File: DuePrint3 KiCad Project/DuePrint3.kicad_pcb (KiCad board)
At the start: 2 copper layers, 208.9 x 75.2 mm, 50 parts, among them J1 MF3.0-2x12-430452412, J10 MF3.0-1x2-436500215, J11 2.54Header-1x2-M, J12 2.54Header-1x2-M, J13 EHT-125-01-S-D, J14 EHT-110-01-S-D, J15 EHT-125-01-S-D, J2 2.54Header-1x16-F, J3 2.54Header-1x16-F, J4 6P2C, J5 6P2C, J6 2.54Header-1x3-M, J7 MF3.0-1x2-436500215, J8 MF3.0-1x8-436500815, J9 MF3.0-2x9-430451812, U1 SN74AHCT125DR

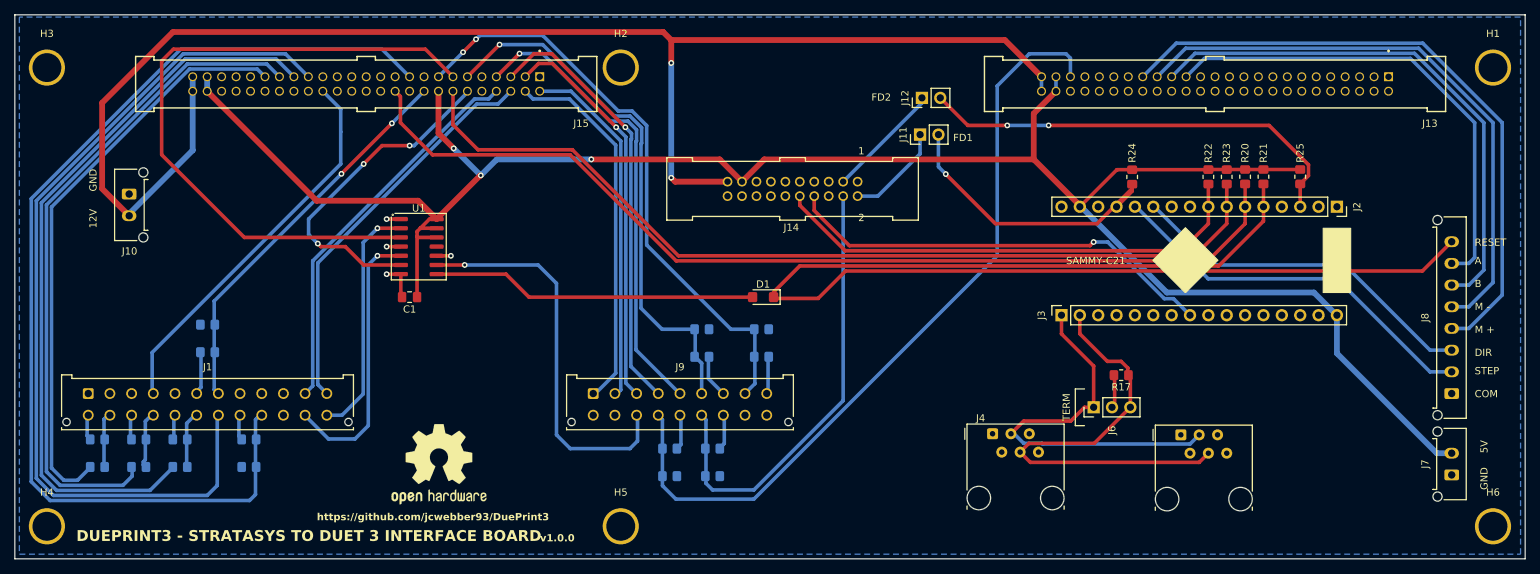
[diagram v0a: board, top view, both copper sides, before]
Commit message: v2.2.0 initial release
Primarily focused on KiCad files, configuration files, build instructions.
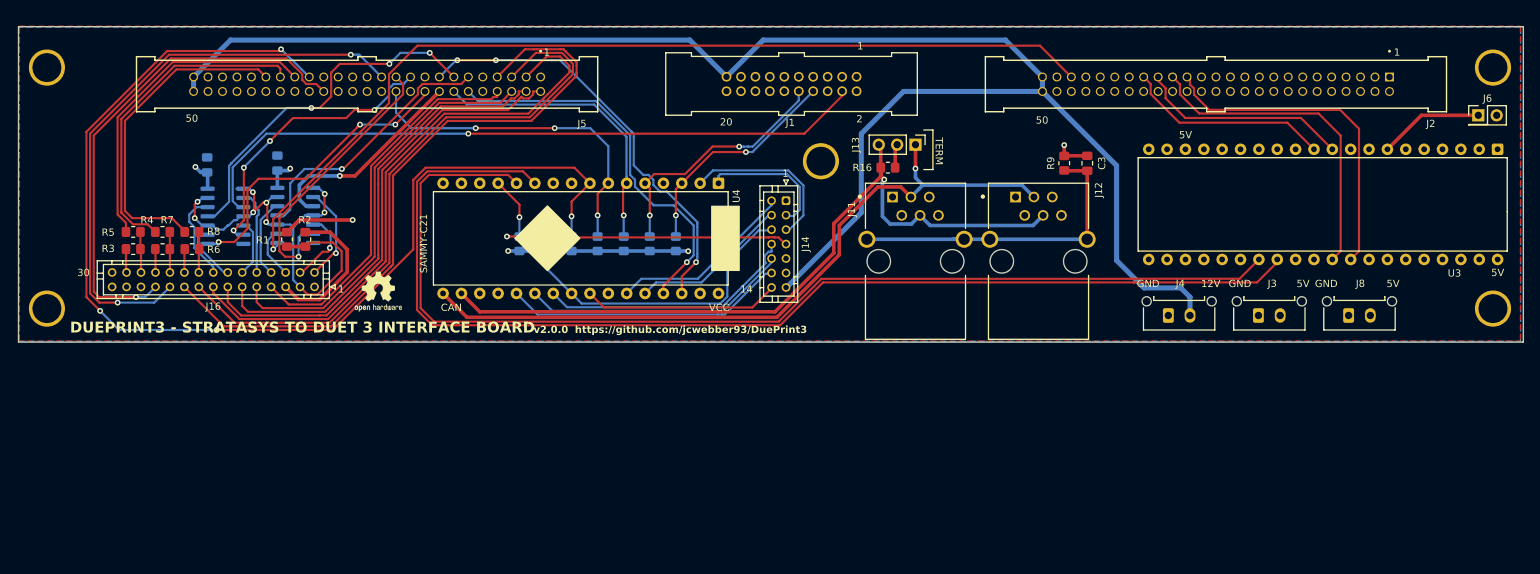
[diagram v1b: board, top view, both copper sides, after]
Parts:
- removed D1: 100v 1A, Diode_SMD:D_SMF
- removed H6: MountingHole_Pad, Stratasys Adapter:MountingHole_4.00mm_Pad
- removed J10, J7: MF3.0-1x2-436500215, Connector_Molex:Molex_Micro-Fit_3.0_43650-0215_1x02_P3.00mm_Vertical
- removed J15: EHT-125-01-S-D, DuePrint3-Lib:SAMTEC_EHT-125-01-S-D
- removed J9: MF3.0-2x9-430451812, Connector_Molex:Molex_Micro-Fit_3.0_43045-1812_2x09_P3.00mm_Vertical
- removed R18: 31.6K, Resistor_SMD:R_0805_2012Metric_Pad1.20x1.40mm_HandSolder
- removed R19: 3740, Resistor_SMD:R_0805_2012Metric_Pad1.20x1.40mm_HandSolder
- removed R20, R21, R22, R23, R24, R25: 10k, Resistor_SMD:R_0805_2012Metric_Pad1.20x1.40mm_HandSolder
- removed the REF** at (114.6, 86.6)
- added C2: 0.1 µF, Capacitor_SMD:C_0805_2012Metric_Pad1.18x1.45mm_HandSolder, B.Cu at (82.5, 45.2)
- added C3: 10n 25V, Capacitor_SMD:C_0805_2012Metric_Pad1.18x1.45mm_HandSolder, F.Cu at (204.2, 45.0)
- added J16: Conn_02x15_Odd_Even, Connector_JST:JST_PHD_B30B-PHDSS_2x15_P2.00mm_Vertical, F.Cu at (97.3, 62.1)
- added REF**: OSHW-Logo2_7.3x6mm_SilkScreen, Symbol:OSHW-Logo2_7.3x6mm_SilkScreen, F.Cu at (106.2, 62.7)
- added U2: SN74AHCT125DR, Package_SO:SOIC-14_3.9x8.7mm_P1.27mm, B.Cu at (85.0, 52.3)
- added U3: BLACKPILL, DuePrint3-Lib:STM32 BLACKPILL, F.Cu at (240.2, 50.5)
- added U4: SAMMY-C21, DuePrint3-Lib:SAMMY-C21, F.Cu at (153.2, 47.8)
- C1: moved to B.Cu
- J1: value MF3.0-2x12-430452412 -> EHT-110-01-S-D; footprint Connector_Molex:Molex_Micro-Fit_3.0_43045-2412_2x12_P3.00mm_Vertical -> DuePrint3-Lib:EHT-110-01-XX-D
- J11, J12: value 2.54Header-1x2-M -> 6P2C; footprint Connector_PinHeader_2.54mm:PinHeader_1x02_P2.54mm_Vertical -> DuePrint3-Lib:BEL_SS-6466S-A-PG1
- J13: value EHT-125-01-S-D -> 2.54Header-1x3-M; footprint DuePrint3-Lib:SAMTEC_EHT-125-01-S-D -> Connector_PinHeader_2.54mm:PinHeader_1x03_P2.54mm_Vertical
- J14: value EHT-110-01-S-D -> Conn_02x07_Top_Bottom; footprint DuePrint3-Lib:EHT-110-01-XX-D -> Connector_JST:JST_PHD_B14B-PHDSS_2x07_P2.00mm_Vertical
- J2: value 2.54Header-1x16-F -> EHT-125-01-S-D; footprint Connector_PinSocket_2.54mm:PinSocket_1x16_P2.54mm_Vertical -> DuePrint3-Lib:SAMTEC_EHT-125-01-S-D
- J3: value 2.54Header-1x16-F -> MF3.0-1x2-436500215; footprint Connector_PinSocket_2.54mm:PinSocket_1x16_P2.54mm_Vertical -> Connector_Molex:Molex_Micro-Fit_3.0_43650-0215_1x02_P3.00mm_Vertical
- J4: value 6P2C -> MF3.0-1x2-436500215; footprint Connector_RJ:RJ12_Amphenol_54601-x06_Horizontal -> Connector_Molex:Molex_Micro-Fit_3.0_43650-0215_1x02_P3.00mm_Vertical
- J5: value 6P2C -> EHT-125-01-S-D; footprint Connector_RJ:RJ12_Amphenol_54601-x06_Horizontal -> DuePrint3-Lib:SAMTEC_EHT-125-01-S-D
- J6: value 2.54Header-1x3-M -> Conn_01x02; footprint Connector_PinHeader_2.54mm:PinHeader_1x03_P2.54mm_Vertical -> Connector_PinHeader_2.54mm:PinHeader_2x01_P2.54mm_Vertical
- J8: value MF3.0-1x8-436500815 -> MF3.0-1x2-436500215; footprint Connector_Molex:Molex_Micro-Fit_3.0_43650-0815_1x08_P3.00mm_Vertical -> Connector_Molex:Molex_Micro-Fit_3.0_43650-0215_1x02_P3.00mm_Vertical
- R1: value 2K -> 3740; moved to F.Cu
- R10, R12, R14: value 3740 -> 10k
- R11, R13, R15: value 31.6K -> 10k
- R16: value 3740 -> 120; moved to F.Cu
- R17: value 120 -> 10k; moved to B.Cu
- R2: value 1K -> 31.6K; moved to F.Cu
- R3, R4, R5: moved to F.Cu
- R6: value 1K -> 2K; moved to F.Cu
- R7: value 31.6K -> 1K; moved to F.Cu
- R8: value 3740 -> 1K; moved to F.Cu
- R9: value 31.6K -> 100K; moved to F.Cu
- U1: footprint PCM_Package_SO_AKL:SOIC-14_3.9x8.7mm_P1.27mm -> Package_SO:SOIC-14_3.9x8.7mm_P1.27mm; moved to B.Cu
- moved H5 124.4 mm to (260.4, 65.1)
- moved J5 122.6 mm to (104.6, 34.1), turned to 180 degrees
- moved R9 121.3 mm to (201.0, 45.0), turned to 90 degrees
- moved J1 106.3 mm to (163.3, 34.0), turned to 180 degrees
- moved R17 81.7 mm to (129.3, 56.1), turned to -90 degrees
- moved R7 76.6 mm to (76.3, 54.5)
- moved R8 71.8 mm to (80.4, 54.5), turned to 180 degrees
- moved J6 66.8 mm to (258.3, 38.4), turned to 0 degrees
- moved R12 60.3 mm to (140.1, 56.1), turned to -90 degrees
- moved R11 55.3 mm to (136.5, 56.1), turned to 90 degrees
- moved R16 52.3 mm to (176.7, 45.6)
- moved R10 51.6 mm to (132.9, 56.1), turned to 90 degrees
- moved J13 42.3 mm to (180.5, 42.4), turned to -90 degrees
- moved R2 39.0 mm to (96.1, 55.5), turned to -90 degrees
- moved R14 35.5 mm to (125.7, 56.1), turned to 90 degrees
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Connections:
- J1 pad 10: unconnected-(J1-Pin_10-Pad10) -> Print Head Support Toggle SW
- J1 pad 11: PRINT BED TOUCH PR LIM SW -> unconnected-(J1-Pin_11-Pad11)
- J1 pad 12: Z-Axis End of Travel Lim SW -> unconnected-(J1-Pin_12-Pad12)
- J1 pad 13: /T0 -> GND
- J1 pad 14: /T0 -> unconnected-(J1-Pin_14-Pad14)
- J1 pad 15: /T2 VSSA -> GND
- J1 pad 16: /T2 -> GND
- J1 pad 17: /T1 VSSA -> +5V
- J1 pad 18: /T1 -> GND
- J1 pad 19: CHAMBER TEMP ALARM -> +12V
- J1 pad 20: VD EXTRUDER SUPPORT HEATER ENABLE -> GND
- J1 pad 4: PRINT HEAD TEMP ALARM -> PRINT HEAD BLOWER ENABLE
- J1 pad 5: unconnected-(J1-Pin_5-Pad5) -> GND
- J1 pad 6: VD EXTRUDER MODEL HEATER ENABLE -> unconnected-(J1-Pin_6-Pad6)
- J1 pad 7: EMHE PWM -> unconnected-(J1-Pin_7-Pad7)
- J1 pad 8: unconnected-(J1-Pin_8-Pad8) -> Print Head Model Toggle SW
- J1 pad 9: unconnected-(J1-Pin_9-Pad9) -> GND
- J11 pad 1: FD1 -> unconnected-(J11-Pad1)
- J11 pad 2: Net-(J11-Pin_2) -> unconnected-(J11-Pad2)
- J12 pad 1: FD2 -> unconnected-(J12-Pad1)
- J12 pad 2: Net-(J12-Pin_2) -> unconnected-(J12-Pad2)
- J13 pad 1: unconnected-(J13-Pin_1-Pad1) -> CAN0H
- J13 pad 2: GND -> Net-(J13-Pin_2)
- J13 pad 3: unconnected-(J13-Pin_3-Pad3) -> CAN0L
- J14 pad 10: Print Head Support Toggle SW -> SPR6
- J14 pad 11: unconnected-(J14-Pin_11-Pad11) -> GND
- J14 pad 12: unconnected-(J14-Pin_12-Pad12) -> SPR7
- J14 pad 13: GND -> +12V
- J14 pad 14: unconnected-(J14-Pin_14-Pad14) -> SPR8
- J14 pad 2: FD1 -> SPR4
- J14 pad 3: FD2 -> SPR1
- J14 pad 4: PHBE PWM -> SPR3
- J14 pad 5: GND -> SPR2
- J14 pad 6: unconnected-(J14-Pin_6-Pad6) -> I_SPR2
- J14 pad 7: unconnected-(J14-Pin_7-Pad7) -> I_SPR1
- J14 pad 8: Print Head Model Toggle SW -> SPR5
- J14 pad 9: GND -> +5V
- J2 pad 10: unconnected-(J2-Pin_10-Pad10) -> GND
- J2 pad 11: DIR -> unconnected-(J2-Pin_11-Pad11)
- J2 pad 12: STEP -> GND
- J2 pad 13: Net-(J11-Pin_2) -> GND
- J2 pad 14: unconnected-(J2-Pin_14-Pad14) -> GND
- J2 pad 15: +5V -> unconnected-(J2-Pin_15-Pad15)
- J2 pad 2: unconnected-(J2-Pin_2-Pad2) -> GND
- J2 pad 3: Net-(J12-Pin_2) -> unconnected-(J2-Pin_3-Pad3)
- J2 pad 4: unconnected-(J2-Pin_4-Pad4) -> GND
- J2 pad 5: GECKO ERROR -> unconnected-(J2-Pin_5-Pad5)
- J2 pad 6: HEAD THERMOSTAT STATUS -> GND
- J2 pad 7: DOOR SWITCH -> unconnected-(J2-Pin_7-Pad7)
- J2 pad 8: Print Head Support Toggle SW -> GND
- J3 pad 1: CAN0H -> GND
- J3 pad 2: CAN0L -> +5V
- J4 pad 1: unconnected-(J4-Pad1) -> GND
- J4 pad 2: unconnected-(J4-Pad2) -> +12V
- J5 pad 1: unconnected-(J5-Pad1) -> GND
- J5 pad 2: unconnected-(J5-Pad2) -> X-Axis End of Travel Lim SW
- J5 pad 3: CAN0H -> X-AXIS HOME LIM SW
- J5 pad 4: CAN0L -> Y-Axis End of Travel Lim SW
- J5 pad 5: unconnected-(J5-Pad5) -> Y-AXIS HOME LIM SW
- J5 pad 6: unconnected-(J5-Pad6) -> Z-Axis End of Travel Lim SW
- J6 pad 1: CAN0H -> Net-(J6-Pin_1)
- J6 pad 2: Net-(J6-Pin_2) -> GND
- J8 pad 2: STEP -> +5V
- R1 pad 1: /T2 VSSA -> 48v RTN PWM
- R1 pad 2: /T2 -> GND
- R10 pad 1: EMHE PWM -> +5V
- R10 pad 2: GND -> CHAMBER TEMP ALARM
- R11 pad 1: VD EXTRUDER SUPPORT HEATER ENABLE -> +5V
- R11 pad 2: ESHE PWM -> HEAD THERMOSTAT STATUS
- R12 pad 1: ESHE PWM -> DOOR SWITCH
- R12 pad 2: GND -> +5V
- R13 pad 1: VD PRINT BED TOUCH PR PWR EN -> Print Head Support Toggle SW
- R13 pad 2: PBTPE PWM -> +5V
- R14 pad 1: PBTPE PWM -> +5V
- R14 pad 2: GND -> I_SPR1
- R15 pad 1: VD MOTOR ENABLE -> +5V
- R15 pad 2: MOTOR ENABLE -> Print Head Model Toggle SW
- R16 pad 1: MOTOR ENABLE -> CAN0L
- R16 pad 2: GND -> Net-(J13-Pin_2)
- R17 pad 1: CAN0L -> +5V
- R17 pad 2: Net-(J6-Pin_2) -> I_SPR2
- R2 pad 1: /T2 -> 48v
- R2 pad 2: PRINT HEAD SUPP THEM -> 48v RTN PWM
- R3 pad 1: /T0 -> /VSSA1
- R3 pad 2: /T0 -> /T1
- R4 pad 1: /T1 VSSA -> /VSSA2
- R4 pad 2: /T1 -> /T2
- R5 pad 2: PRINT HEAD MODEL THEM -> PRINT HEAD MODEL THERM
- R6 pad 1: /T0 -> /VSSA0
- R6 pad 2: CHAMBER TEMP THERM -> /T0
- R7 pad 1: VD CHAMBER HEATER ENABLE -> /T2
- R7 pad 2: CHAMBER HEATER ENABLE -> PRINT HEAD SUPP THERM
- R8 pad 1: CHAMBER HEATER ENABLE -> /T0
- R8 pad 2: GND -> CHAMBER TEMP THERM
- R9 pad 1: VD EXTRUDER MODEL HEATER ENABLE -> Net-(C3-Pad1)
- R9 pad 2: EMHE PWM -> GND
- U1 pad 1: GND -> 48v RTN PWM
- U1 pad 10: GND -> 48v RTN PWM
- U1 pad 11: unconnected-(U1-4Y-Pad11) -> CHAMBER HEATER ENABLE
- U1 pad 12: +5V -> LS CHAMBER HEATER ENABLE
- U1 pad 13: +5V -> 48v RTN PWM
- U1 pad 2: LS DOOR SOLENOID ENABLE -> LS 120V ON
- U1 pad 3: DOOR SOLENOID ENABLE -> 120V ON
- U1 pad 4: GND -> 48v RTN PWM
- U1 pad 5: LS LED Lights Enable -> LS POWER ON
- U1 pad 6: LED Lights Enable -> POWER ON
- U1 pad 8: Net-(D1-A) -> MOTOR ENABLE
- U1 pad 9: LS GECKO RESET -> LS MOTOR ENABLE
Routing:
- net +5V: track 284.3 -> 35.2 mm, vias 3 -> 4
- net GECKO ERROR: track 174.8 -> 0.00 mm
- net ESHE PWM: track 145.5 -> 0.00 mm
- net DIR: track 49.5 -> 159.2 mm
- net PRINT HEAD MODEL THEM: track 102.4 -> 0.00 mm
- net STEP: track 53.3 -> 151.8 mm
- net PRINT HEAD BLOWER ENABLE: track 0.00 -> 95.5 mm, vias 0 -> 1
- net PRINT HEAD SUPP THEM: track 92.4 -> 0.00 mm
- net HEAD THERMOSTAT STATUS: track 137.0 -> 47.3 mm, vias 0 -> 3
- net DOOR SWITCH: track 126.5 -> 40.5 mm, vias 0 -> 1
- net PBTPE PWM: track 82.1 -> 0.00 mm, vias 2 -> 0
- net POWER I/O: track 0.00 -> 80.7 mm, vias 0 -> 2
- net 48v RTN PWM: track 0.00 -> 68.2 mm, vias 0 -> 8
- net PHBE PWM: track 62.2 -> 0.00 mm
- net Net-(J12-Pin_2): track 61.0 -> 0.00 mm, vias 2 -> 0
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- added copper zone on F.Cu, net +5V
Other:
- board size 208.9 x 75.2 mm -> 208.2 x 43.6 mm
- board text added: "1"
- board text added: "14"
- board text added: "20"
- board text added: "30"
- board text added: "50"
- board text added: "CAN"
- board text added: "VCC"
- board text added: "v2.0.0"
- board text removed: "A"
- board text removed: "B"
- board text removed: "COM"
- board text removed: "DIR"
- board text removed: "FD1"
- board text removed: "FD2"
- board text removed: "M +"
- board text removed: "M -"
- board text removed: "RESET"
- board text removed: "STEP"
- board text removed: "v1.0.0"
